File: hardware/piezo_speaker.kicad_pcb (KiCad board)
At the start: 2 copper layers, 30 x 25 mm, 24 parts, among them P1 CON-SENSOR, Q1 2N7002P, U1 M24C64, U2 MCP4651-104E/ST, U3 ICM7555, U4 DRILL, U5 DRILL, U6 DRILL, U7 DRILL

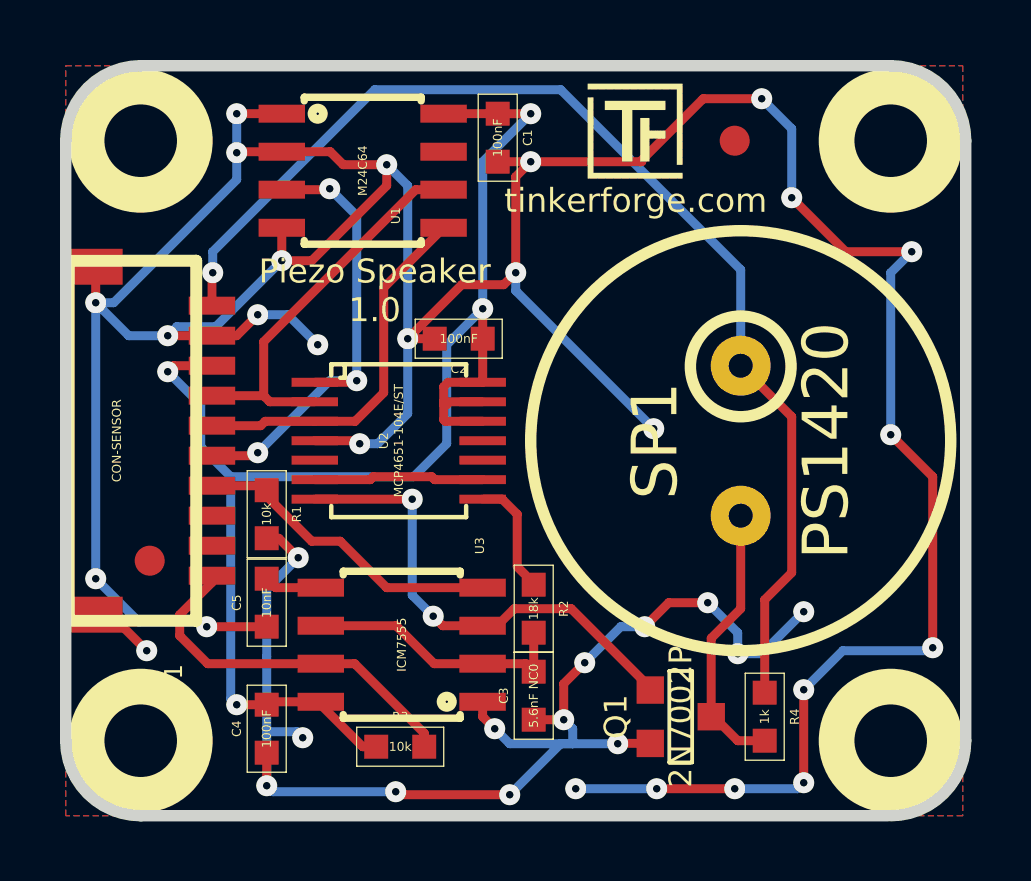
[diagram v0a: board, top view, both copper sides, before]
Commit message: Add 3d information
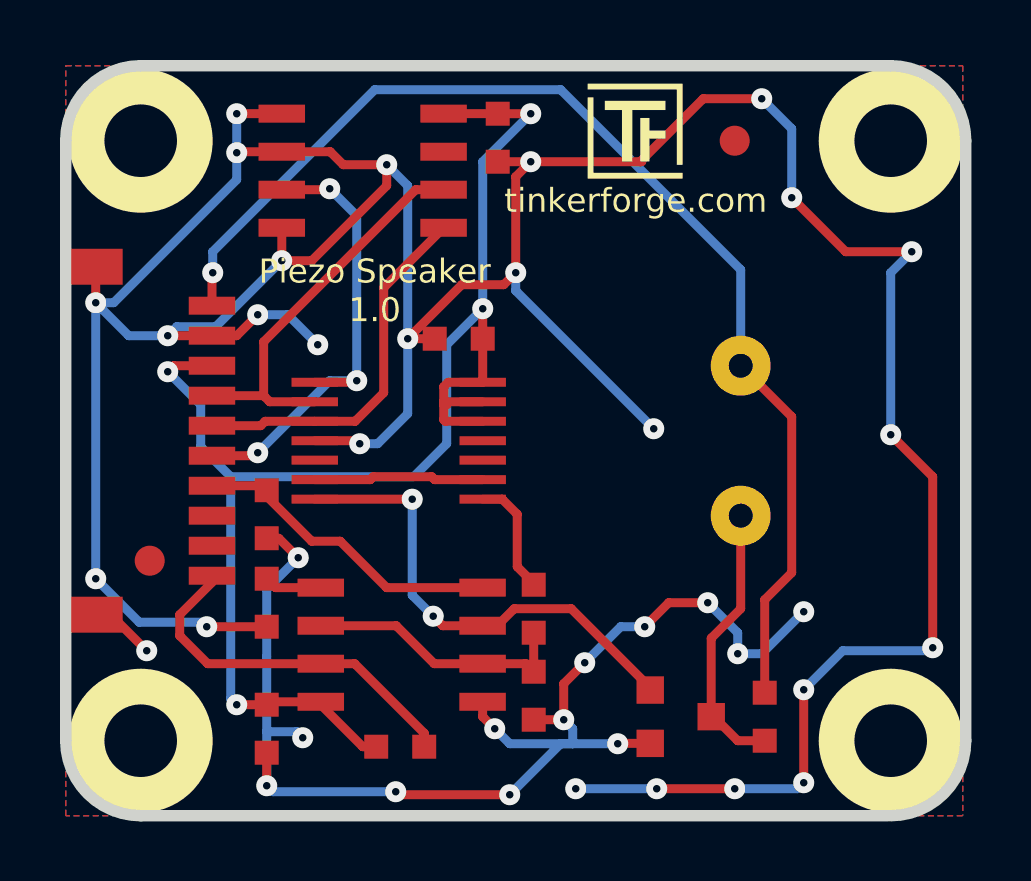
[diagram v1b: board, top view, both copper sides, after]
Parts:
- C1, C2, C3, C4, C5: footprint 0603 -> kicad-libraries:C0603
- Fiducial_Mark (x2): footprint Fiducial_Mark -> kicad-libraries:Fiducial_Mark
- G***: footprint Logo_31x31 -> kicad-libraries:Logo_31x31
- P1: footprint CON-SENSOR -> kicad-libraries:CON-SENSOR
- Q1: footprint SOT23GDS -> kicad-libraries:SOT23GDS
- R1, R2, R3, R4: footprint 0603 -> kicad-libraries:R0603
- SP1: footprint PS1420 -> kicad-libraries:PS1420
- U1, U3: footprint SOIC8 -> kicad-libraries:SOIC8
- U2: footprint TSSOP14 -> kicad-libraries:TSSOP14
- U4, U5, U6, U7: footprint DRILL_NP -> kicad-libraries:DRILL_NP
- VAL: footprint WEEE_7mm -> kicad-libraries:WEEE_7mm
- VAL: footprint CE_5mm -> kicad-libraries:CE_5mm
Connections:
- P1 pad 8: (no net) -> Net-(P1-Pad8)
- P1 pad 9: (no net) -> Net-(P1-Pad9)
- U1 pad 7: (no net) -> Net-(U1-Pad7)
- U2 pad 10: (no net) -> Net-(U2-Pad10)
- U2 pad 11: (no net) -> Net-(U2-Pad11)
- U2 pad 5: (no net) -> Net-(U2-Pad5)
